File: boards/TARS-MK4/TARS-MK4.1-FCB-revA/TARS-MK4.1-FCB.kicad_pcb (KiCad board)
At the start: 2 copper layers, 86 x 79.1 mm, 70 parts, among them J101 U.FL, J102 Molex_SlimStack_2091680401_2x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, J103 Molex_SlimStack_2091680401_2x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, J104 Molex_SlimStack_Plug_55091047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, J105 Molex_SlimStack_Plug_55091047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, J106 Conn_01x03, J107 Conn_01x02, J108 Conn_01x06, J109 Conn_01x03, Q101 SSM3K16FU, SW101 FSMSM Switch, U101 MS5611-01BA03, U102 LSM6DSLTR, U103 MAX-M10S, U104 BNO086, U105 LIS3MDL, U106 KX134-1211, U107 Teensy4.1, U108 BME688, Y101 32.768kHz

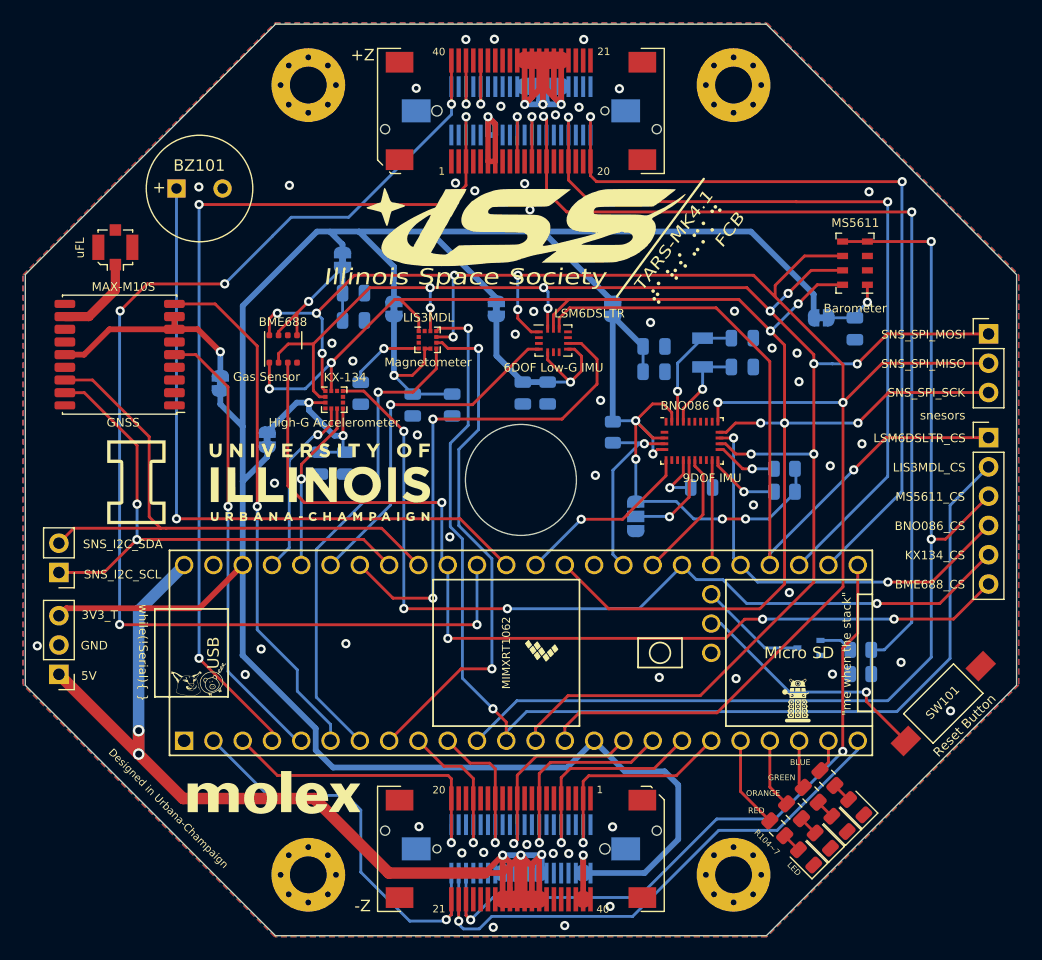
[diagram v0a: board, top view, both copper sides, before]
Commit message: Updated FCB B2B's to match PMB and TELEM
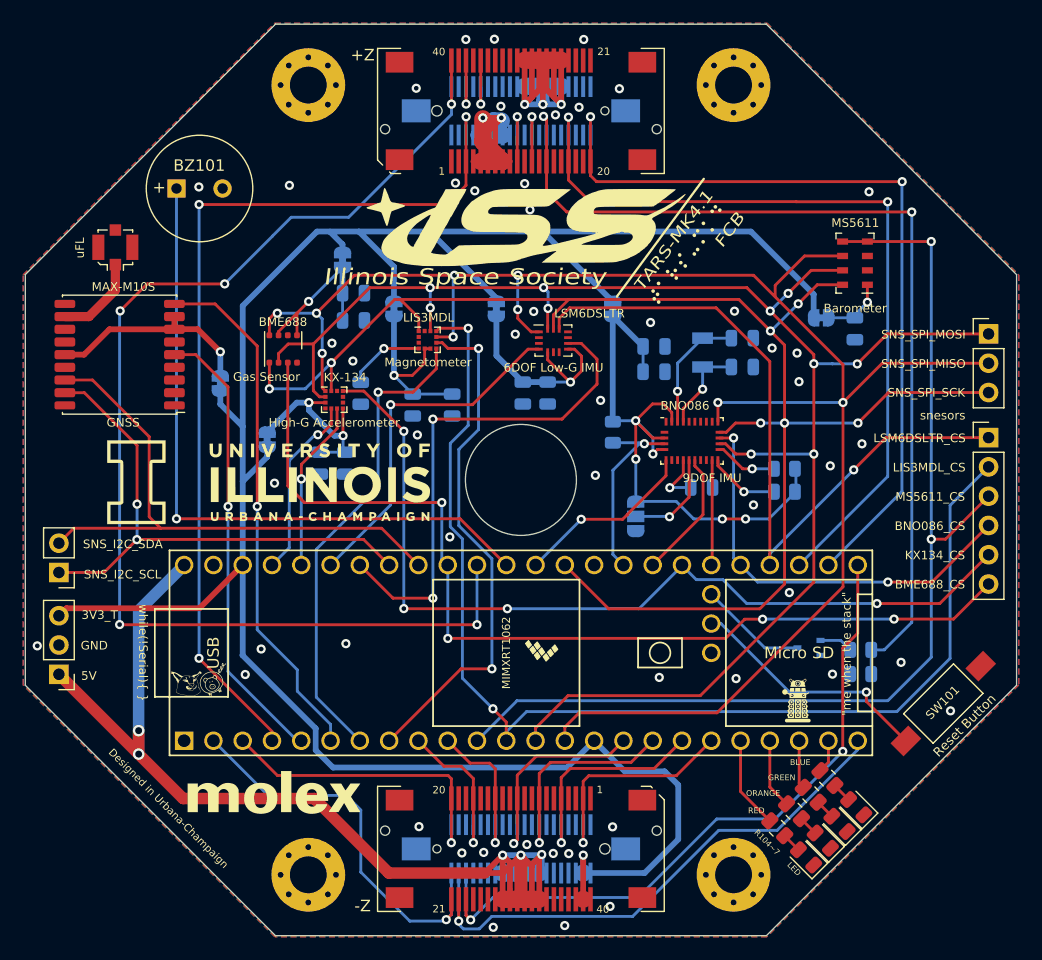
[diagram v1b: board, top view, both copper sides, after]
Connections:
- J102 pad 4: GND -> /VBAT
- J102 pad 5: GND -> /VBAT
- J102 pad 8: GND -> /VBAT
- J102 pad 9: GND -> /VBAT
- J104 pad 4: GND -> /VBAT
- J104 pad 5: GND -> /VBAT
- J104 pad 8: GND -> /VBAT
- J104 pad 9: GND -> /VBAT
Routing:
- net /VBAT: track 12.7 -> 38.3 mm, vias 1 -> 2
